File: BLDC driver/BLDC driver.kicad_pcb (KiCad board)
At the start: 4 copper layers, 75 x 50 mm, 63 parts, among them J1 Screw_Terminal_01x02, J2 Screw_Terminal_01x03, J3 Conn_02x06_Counter_Clockwise, J4 Izlaz ocitavanje struje, Q1 N0436N, Q2 N0436N, Q3 N0436N, Q4 N0436N, Q5 N0436N, Q6 N0436N, U1 MCP8027T-H/Y4X

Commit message: Dodati test point-ovi
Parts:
- added TP1: TestPoint, TestPoint:TestPoint_Pad_D3.0mm, F.Cu at (151.5, 106.0)
- added TP2: TestPoint, TestPoint:TestPoint_Pad_D3.0mm, F.Cu at (147.0, 106.0)
- added TP3: TestPoint, TestPoint:TestPoint_Pad_D3.0mm, F.Cu at (142.5, 106.0)
- added TP4: TestPoint, TestPoint:TestPoint_Pad_D3.0mm, F.Cu at (133.5, 101.5)
- added TP5: TestPoint, TestPoint:TestPoint_Pad_D3.0mm, F.Cu at (138.0, 101.5)
- added TP6: TestPoint, TestPoint:TestPoint_Pad_D3.0mm, F.Cu at (133.5, 106.0)
- added TP7: TestPoint, TestPoint:TestPoint_Pad_D3.0mm, F.Cu at (138.0, 106.0)
- moved R8 10.3 mm to (175.0, 91.5)
- moved R18 10.0 mm to (164.7, 91.5)
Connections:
- C2 pad 2: Net-(J2-Pin_3) -> Net-(J2-Pin_1)
- J2 pad 3: Net-(J2-Pin_3) -> Net-(J2-Pin_1)
- Q3 pad 3: Net-(J2-Pin_3) -> Net-(J2-Pin_1)
- Q6 pad 1: Net-(J2-Pin_3) -> Net-(J2-Pin_1)
- R18 pad 1: Net-(U1-LSC) -> Net-(U1-LSB)
- R8 pad 1: Net-(U1-LSB) -> Net-(U1-LSC)
- U1 pad 28: Net-(J2-Pin_3) -> Net-(J2-Pin_1)
- U1 pad 34: unconnected-(U1-+12V-Pad34) -> Net-(U1-+12V)
- U1 pad 37: unconnected-(U1-LX-Pad37) -> Net-(U1-LX)
- U1 pad 4: unconnected-(U1-LV_OUT2-Pad4) -> Net-(U1-LV_OUT2)
- U1 pad 41: unconnected-(U1-+5V-Pad41) -> Net-(U1-+5V)
- U1 pad 5: unconnected-(U1-HV_IN2-Pad5) -> Net-(U1-HV_IN2)
- U1 pad 6: unconnected-(U1-HV_IN1-Pad6) -> Net-(U1-HV_IN1)
- U1 pad 8: unconnected-(U1-LV_OUT1-Pad8) -> Net-(U1-LV_OUT1)
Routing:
- net Net-(J2-Pin_1): track 17.4 -> 63.4 mm
- net Net-(J2-Pin_3): track 46.0 -> 0.00 mm
- net Net-(U1-LX): track 0.00 -> 35.1 mm, vias 0 -> 2
- net Net-(U1-+12V): track 0.00 -> 32.3 mm, vias 0 -> 2
- net Net-(U1-HV_IN1): track 0.00 -> 32.2 mm, vias 0 -> 2
- net Net-(U1-+5V): track 0.00 -> 31.5 mm, vias 0 -> 2
- net Net-(U1-LV_OUT2): track 0.00 -> 30.4 mm, vias 0 -> 2
- net Net-(U1-LV_OUT1): track 0.00 -> 29.7 mm, vias 0 -> 2
- net Net-(U1-HV_IN2): track 0.00 -> 25.4 mm, vias 0 -> 2
- net I_OUT3: track 23.3 -> 21.3 mm
- net unconnected-(U1-+12V-Pad34): track 1.67 -> 0.00 mm
- net GND: track 166.1 -> 164.7 mm
- net I_OUT1: track 22.7 -> 21.8 mm
- removed copper zone on F.Cu, net Net-(J2-Pin_3)

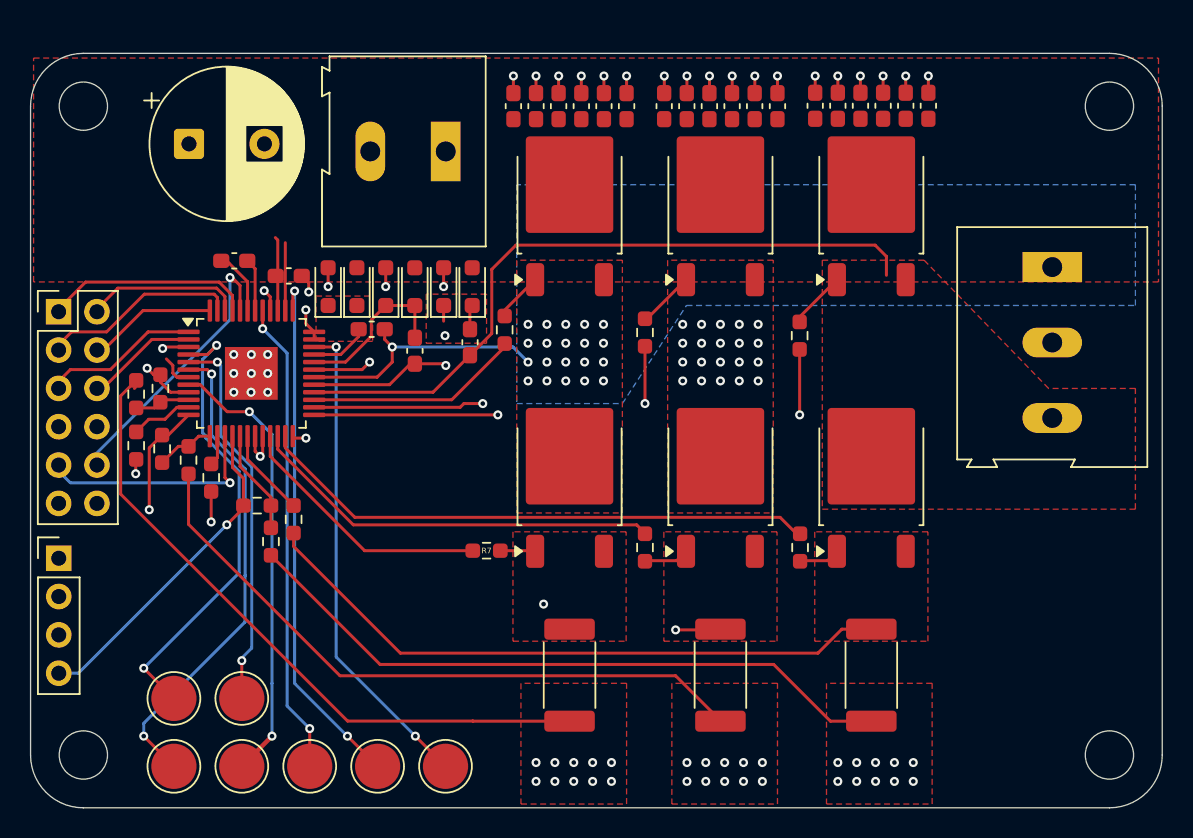
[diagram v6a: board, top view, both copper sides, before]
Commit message: Dodati test pointovi, novi screw konektori i BOM
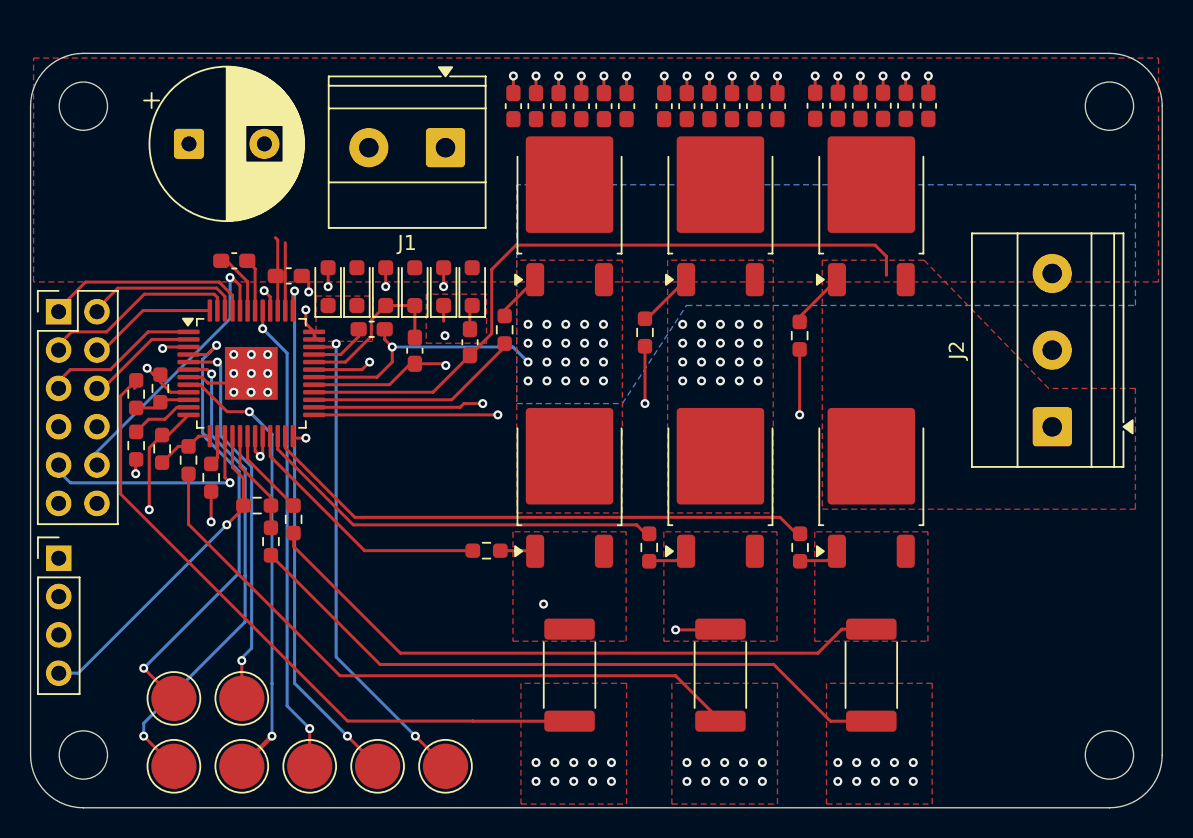
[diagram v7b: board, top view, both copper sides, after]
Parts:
- J1: footprint TerminalBlock:TerminalBlock_Altech_AK300-2_P5.00mm -> TerminalBlock_Phoenix:TerminalBlock_Phoenix_MKDS-1,5-2-5.08_1x02_P5.08mm_Horizontal
- J2: footprint TerminalBlock:TerminalBlock_Altech_AK300-3_P5.00mm -> TerminalBlock_Phoenix:TerminalBlock_Phoenix_MKDS-1,5-3-5.08_1x03_P5.08mm_Horizontal
- moved J2 10.6 mm to (191.7, 83.5), turned to 90 degrees
- moved R18 10.3 mm to (175.0, 91.5)
- moved R8 10.0 mm to (165.0, 91.5)
- moved J1 0.25 mm to (151.5, 65.0)
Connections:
- C2 pad 2: Net-(J2-Pin_1) -> Net-(J2-Pin_3)
- J2 pad 1: Net-(J2-Pin_1) -> Net-(J2-Pin_3)
- Q3 pad 3: Net-(J2-Pin_1) -> Net-(J2-Pin_3)
- Q6 pad 1: Net-(J2-Pin_1) -> Net-(J2-Pin_3)
- R18 pad 1: Net-(U1-LSB) -> Net-(U1-LSC)
- R8 pad 1: Net-(U1-LSC) -> Net-(U1-LSB)
- U1 pad 28: Net-(J2-Pin_1) -> Net-(J2-Pin_3)
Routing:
- net Net-(J2-Pin_1): track 63.4 -> 17.4 mm
- net Net-(J2-Pin_3): track 0.00 -> 46.0 mm
- net GND: track 164.7 -> 166.7 mm
- added copper zone on F.Cu, net Net-(J2-Pin_3)
